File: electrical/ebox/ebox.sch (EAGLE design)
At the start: 0 parts

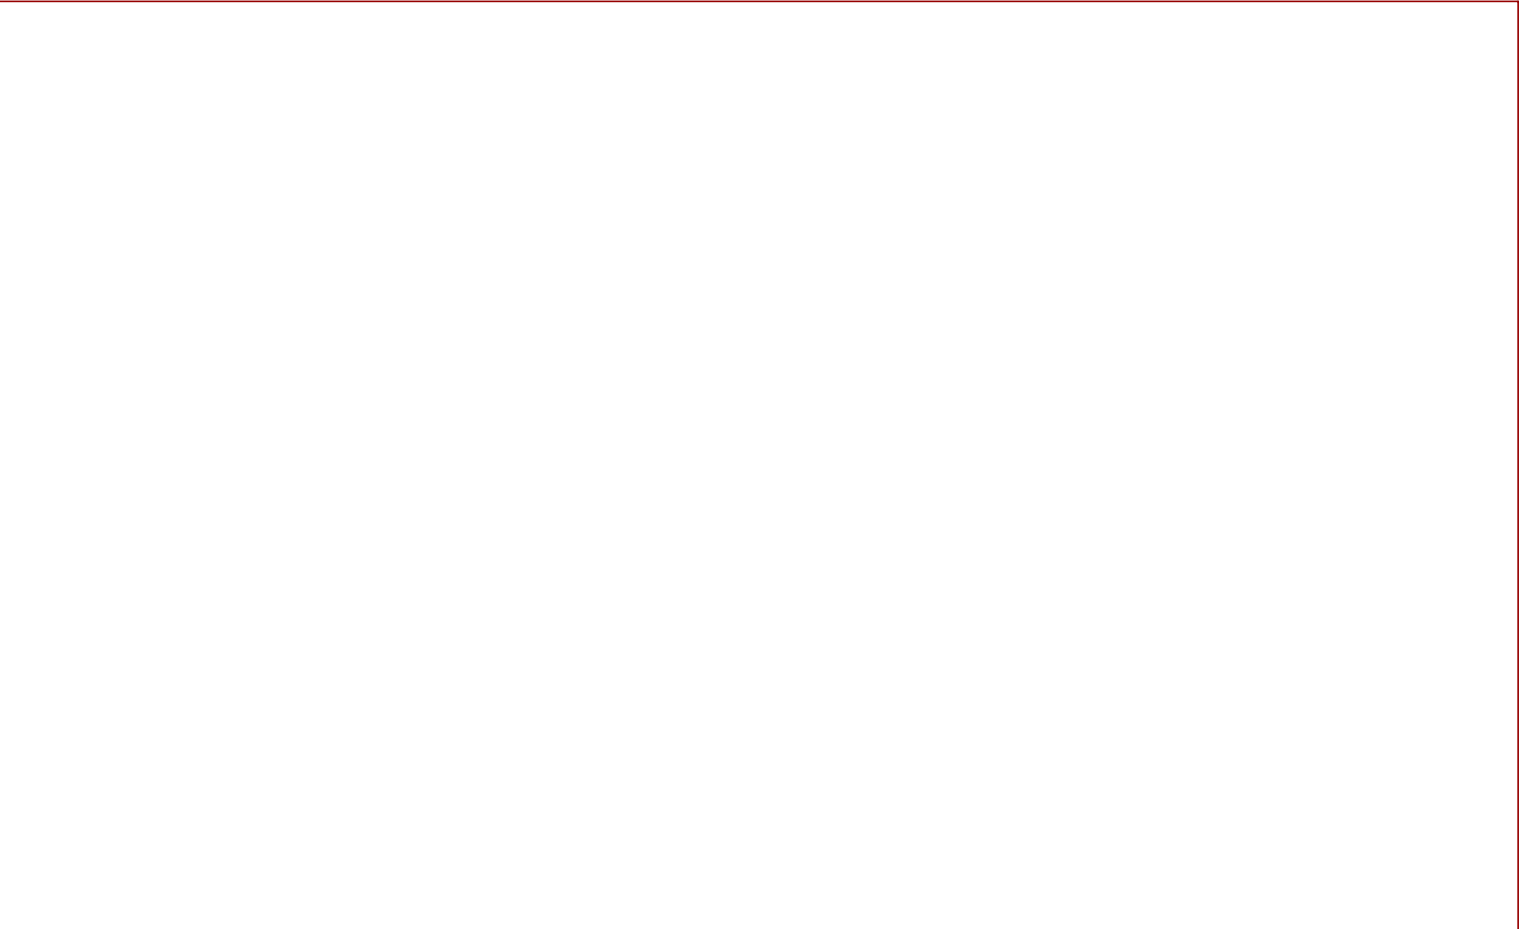
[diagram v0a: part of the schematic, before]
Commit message: Added AVR and connectors to schematic.
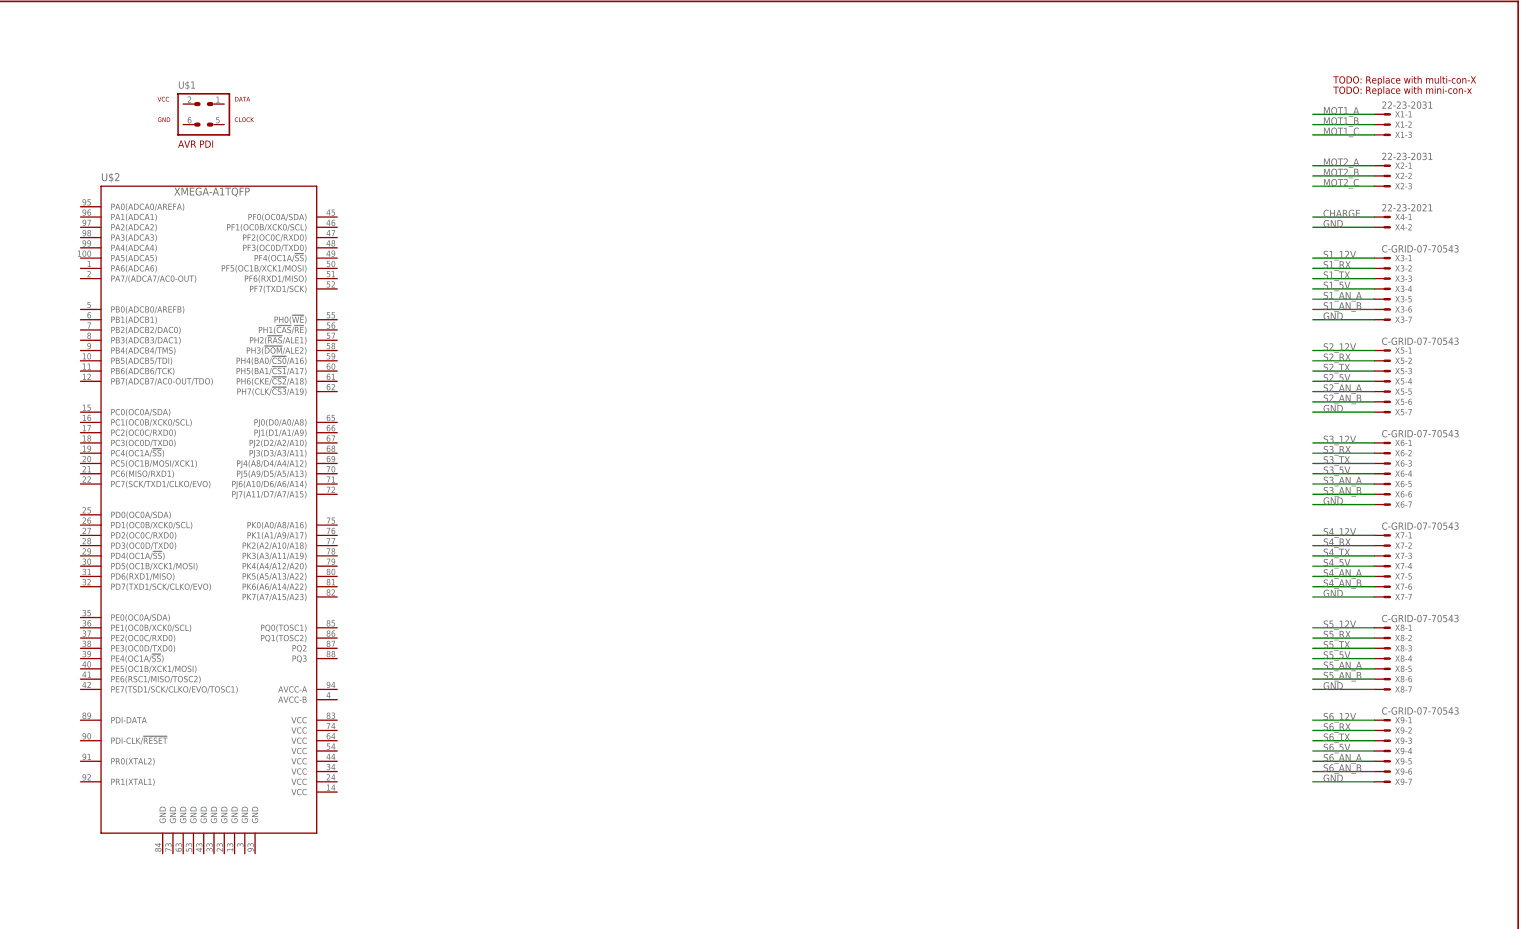
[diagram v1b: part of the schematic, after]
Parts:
- added U$1: AVR-PDIVERT, avr-7:AVR-PDIVERT
- added U$2: XMEGA-A1TQFP, avr-7:XMEGA-A1TQFP
- added X1, X2: 22-23-2031, con-molex:22-23-2031
- added X3, X5, X6, X7, X8, X9: C-GRID-07-70543, con-molex:C-GRID-07-70543
- added X4: 22-23-2021, con-molex:22-23-2021
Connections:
- new net CHARGE: X4-1.S
- new net GND: X3-7.S, X4-2.S, X5-7.S, X6-7.S, X7-7.S, X8-7.S
- new net MOT1_A: X1-1.S
- new net MOT1_B: X1-2.S
- new net MOT1_C: X1-3.S
- new net MOT2_A: X2-1.S
- new net MOT2_B: X2-2.S
- new net MOT2_C: X2-3.S
- new net S1_12V: X3-1.S
- new net S1_5V: X3-4.S
- new net S1_AN_A: X3-5.S
- new net S1_AN_B: X3-6.S
- new net S1_RX: X3-2.S
- new net S1_TX: X3-3.S
- new net S2_12V: X5-1.S
- new net S2_5V: X5-4.S
- new net S2_AN_A: X5-5.S
- new net S2_AN_B: X5-6.S
- new net S2_RX: X5-2.S
- new net S2_TX: X5-3.S
- new net S3_12V: X6-1.S
- new net S3_5V: X6-4.S
- new net S3_AN_A: X6-5.S
- new net S3_AN_B: X6-6.S
- new net S3_RX: X6-2.S
- new net S3_TX: X6-3.S
- new net S4_12V: X7-1.S
- new net S4_5V: X7-4.S
- new net S4_AN_A: X7-5.S
- new net S4_AN_B: X7-6.S
- new net S4_RX: X7-2.S
- new net S4_TX: X7-3.S
- new net S5_12V: X8-1.S
- new net S5_5V: X8-4.S
- new net S5_AN_A: X8-5.S
- new net S5_AN_B: X8-6.S
- new net S5_RX: X8-2.S
- new net S5_TX: X8-3.S
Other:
- note added: "TODO: Replace with mini-con-x"
- note added: "TODO: Replace with multi-con-X"

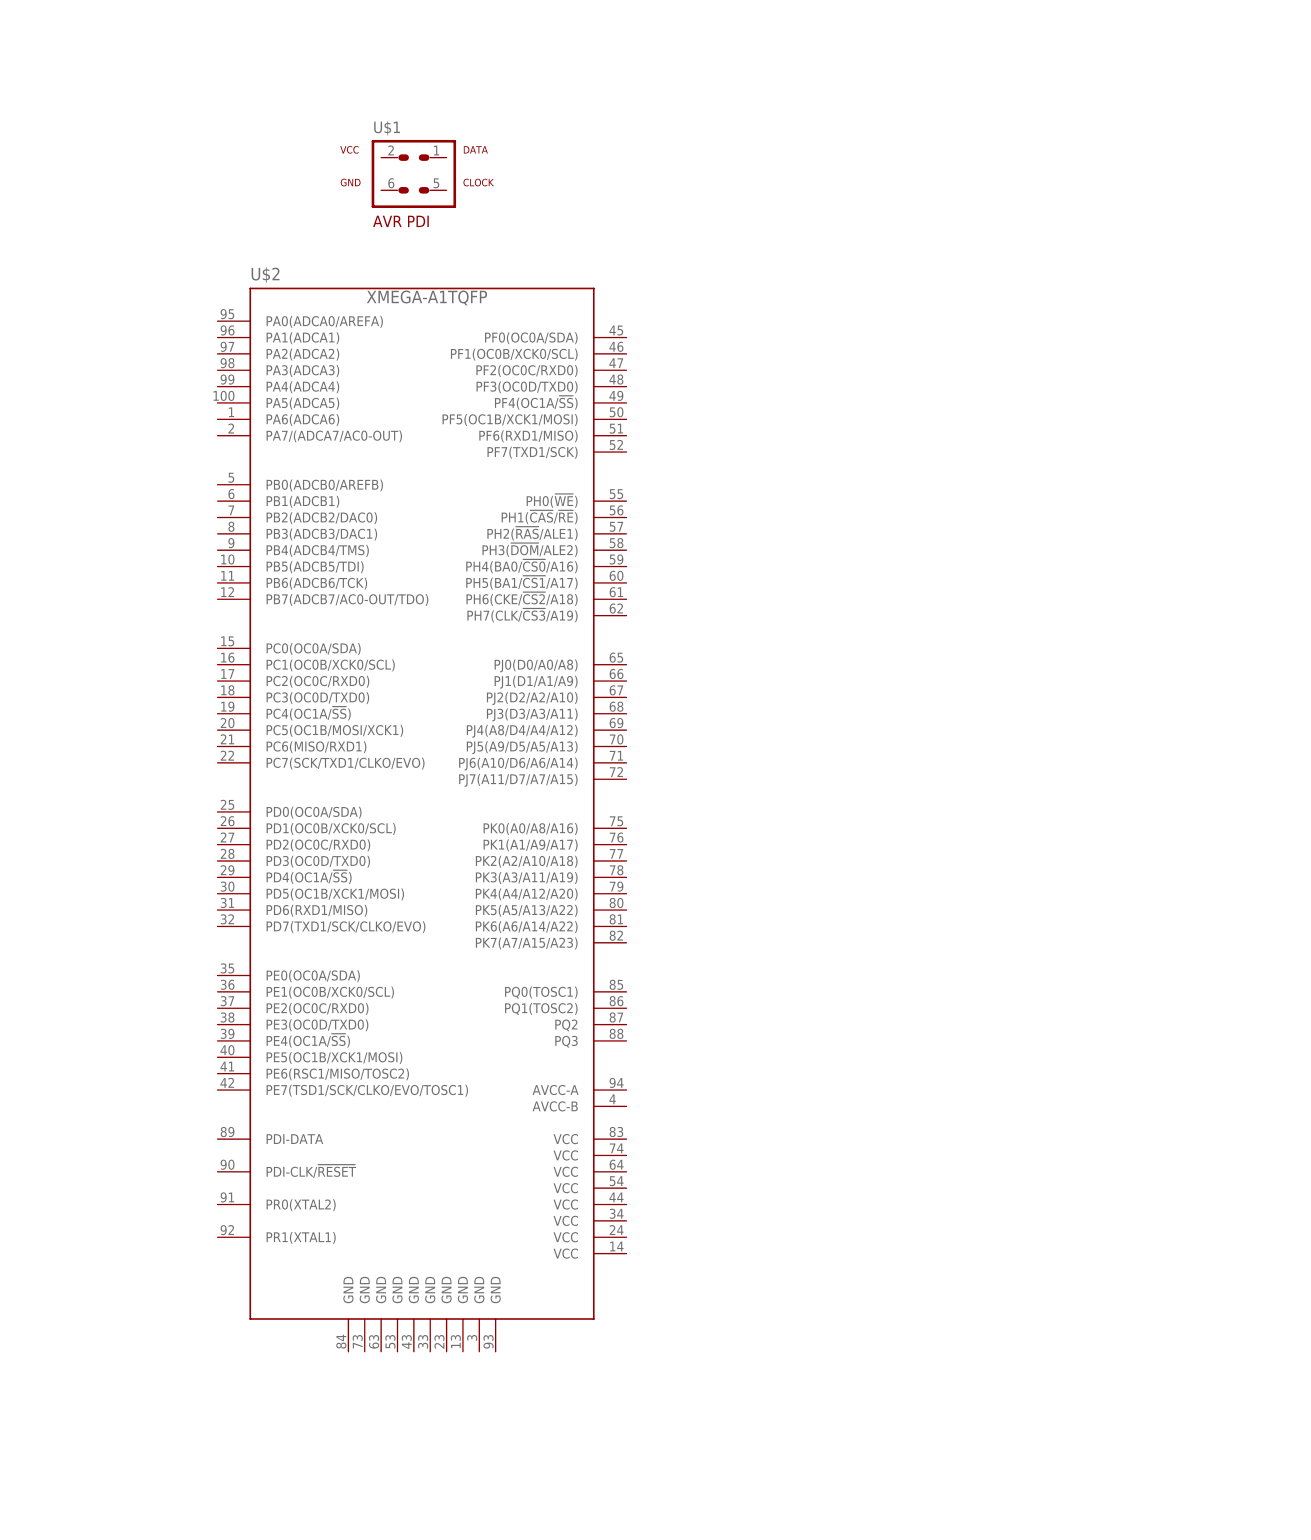
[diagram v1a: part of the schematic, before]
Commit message: Added atmel UC3 library and switched to a USB-host capable 32-bit microcontroller.  We'll see if this is really what we need or not.
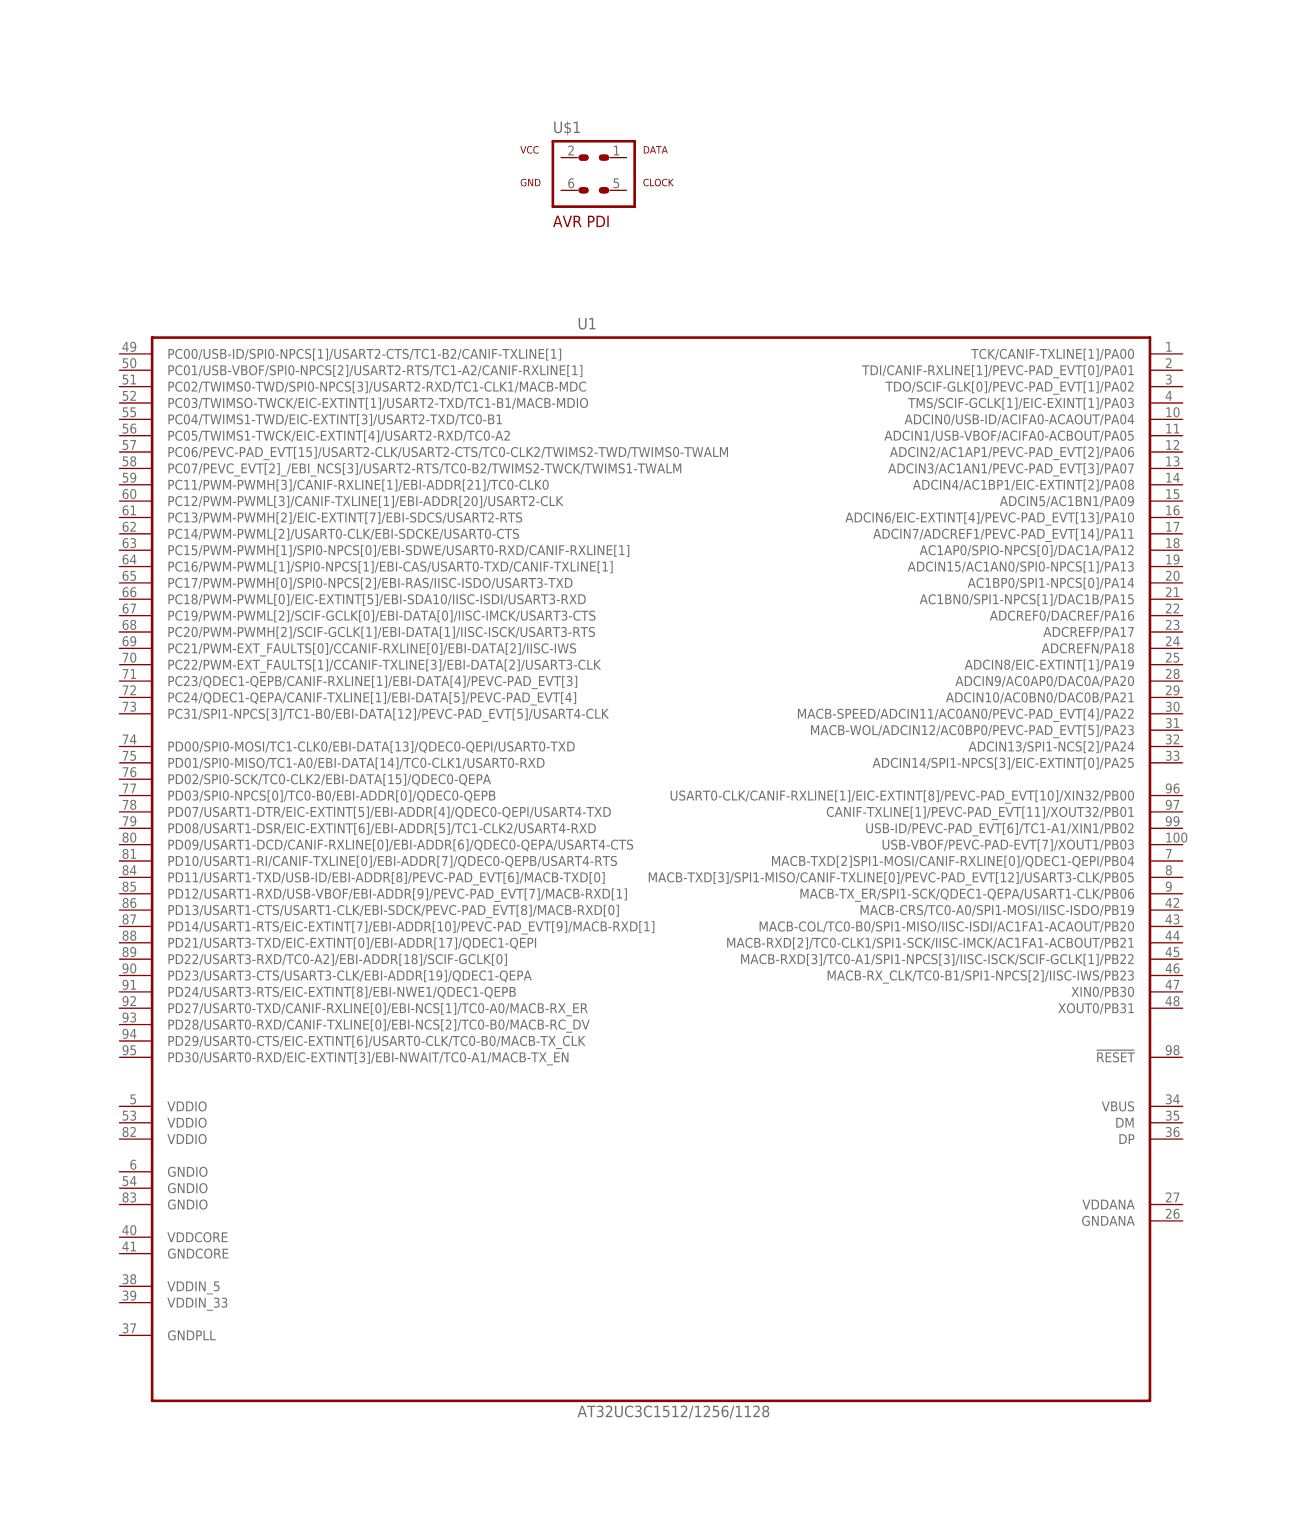
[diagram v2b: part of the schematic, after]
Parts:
- removed U$2: XMEGA-A1TQFP, avr-7:XMEGA-A1TQFP
- added U1: AT32UC3C1512/1256/1128, atmel-avr32-michel:AT32UC3C1512/1256/1128
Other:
- moved on the sheet: U$1
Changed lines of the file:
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@@
 <layer number="51" name="tDocu" color="7" fill="1" visible="no" active="no"/>
 <layer number="52" name="bDocu" color="7" fill="1" visible="no" active="no"/>
+<layer number="56" name="wert" color="7" fill="1" visible="no" active="no"/>
 <layer number="91" name="Nets" color="2" fill="1" visible="yes" active="yes"/>
 <layer number="92" name="Busses" color="1" fill="1" visible="yes" active="yes"/>
@@
 <layer number="97" name="Info" color="7" fill="1" visible="yes" active="yes"/>
 <layer number="98" name="Guide" color="6" fill="1" visible="yes" active="yes"/>
+<layer number="105" name="Beschreib" color="7" fill="1" visible="yes" active="yes"/>
+<layer number="106" name="BGA-Top" color="7" fill="1" visible="yes" active="yes"/>
+<layer number="107" name="BD-Top" color="7" fill="1" visible="yes" active="yes"/>
+<layer number="151" name="HeatSink" color="7" fill="1" visible="yes" active="yes"/>
 <layer number="200" name="200bmp" color="1" fill="10" visible="no" active="no"/>
+<layer number="201" name="201bmp" color="7" fill="1" visible="yes" active="yes"/>
+<layer number="250" name="Descript" color="7" fill="1" visible="yes" active="yes"/>
+<layer number="251" name="SMDround" color="7" fill="1" visible="yes" active="yes"/>
+<layer number="254" name="OrgLBR" color="7" fill="1" visible="yes" active="yes"/>
 </layers>
 <schematic xreflabel="%F%N/%S.%C%R" xrefpart="/%S.%C%R">
@@
 <part name="X9" library="con-molex" deviceset="C-GRID-07" device="-70543"/>
 <part name="U$1" library="avr-7" deviceset="AVR-PDI" device="VERT"/>
-<part name="U$2" library="avr-7" deviceset="XMEGA-A1" device="TQFP"/>
+<part name="U1" library="atmel-avr32-michel" deviceset="AT32UC3C1512/1256/1128" device=""/>
 </parts>
 <sheets>
@@
 <instance part="X9" gate="-6" x="368.3" y="76.2"/>
 <instance part="X9" gate="-7" x="368.3" y="73.66"/>
-<instance part="U$1" gate="G$1" x="76.2" y="238.76"/>
-<instance part="U$2" gate="G$1" x="76.2" y="106.68"/>
+<instance part="U$1" gate="G$1" x="104.14" y="238.76"/>
+<instance part="U1" gate="NAME" x="147.32" y="132.08"/>
 </instances>
 <busses>

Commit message: Added notes for other isolation stuff.
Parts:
- added IC1: MAX3221CUE, maxim:MAX3221CUE
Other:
- note added: "Use the: MAX3323"
- note added: "Use the: SN74LVC1T45"
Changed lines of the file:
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@@
 <setting verticaltext="up"/>
 </settings>
-<grid distance="0.1" unitdist="inch" unit="inch" style="lines" multiple="1" display="yes" altdistance="0.01" altunitdist="inch" altunit="inch"/>
+<grid distance="0.1" unitdist="inch" unit="inch" style="lines" multiple="1" display="no" altdistance="0.01" altunitdist="inch" altunit="inch"/>
 <layers>
 <layer number="1" name="Top" color="4" fill="1" visible="no" active="no"/>
@@
 <part name="U$1" library="avr-7" deviceset="AVR-PDI" device="VERT"/>
 <part name="U1" library="atmel-avr32-michel" deviceset="AT32UC3C1512/1256/1128" device=""/>
+<part name="IC1" library="maxim" deviceset="MAX3221*" device="UE" technology="C"/>
 </parts>
 <sheets>
@@
 <text x="355.6" y="246.38" size="1.778" layer="94">TODO: Replace with multi-con-X</text>
 <text x="355.6" y="243.84" size="1.778" layer="94">TODO: Replace with mini-con-x</text>
+<text x="281.94" y="205.74" size="1.778" layer="94">Use the: SN74LVC1T45</text>
+<text x="281.94" y="200.66" size="1.778" layer="94">Use the: MAX3323</text>
 </plain>
 <instances>
@@
 <instance part="U$1" gate="G$1" x="104.14" y="238.76"/>
 <instance part="U1" gate="NAME" x="147.32" y="132.08"/>
+<instance part="IC1" gate="G$1" x="284.48" y="175.26"/>
 </instances>
 <busses>
